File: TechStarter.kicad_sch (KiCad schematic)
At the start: 17 parts, among them J1 Conn_01x04_Socket, J2 Conn_01x04_Socket, U1 STM32F446RETx, U2 TMC2209-LA, U3 TMC2209-LA

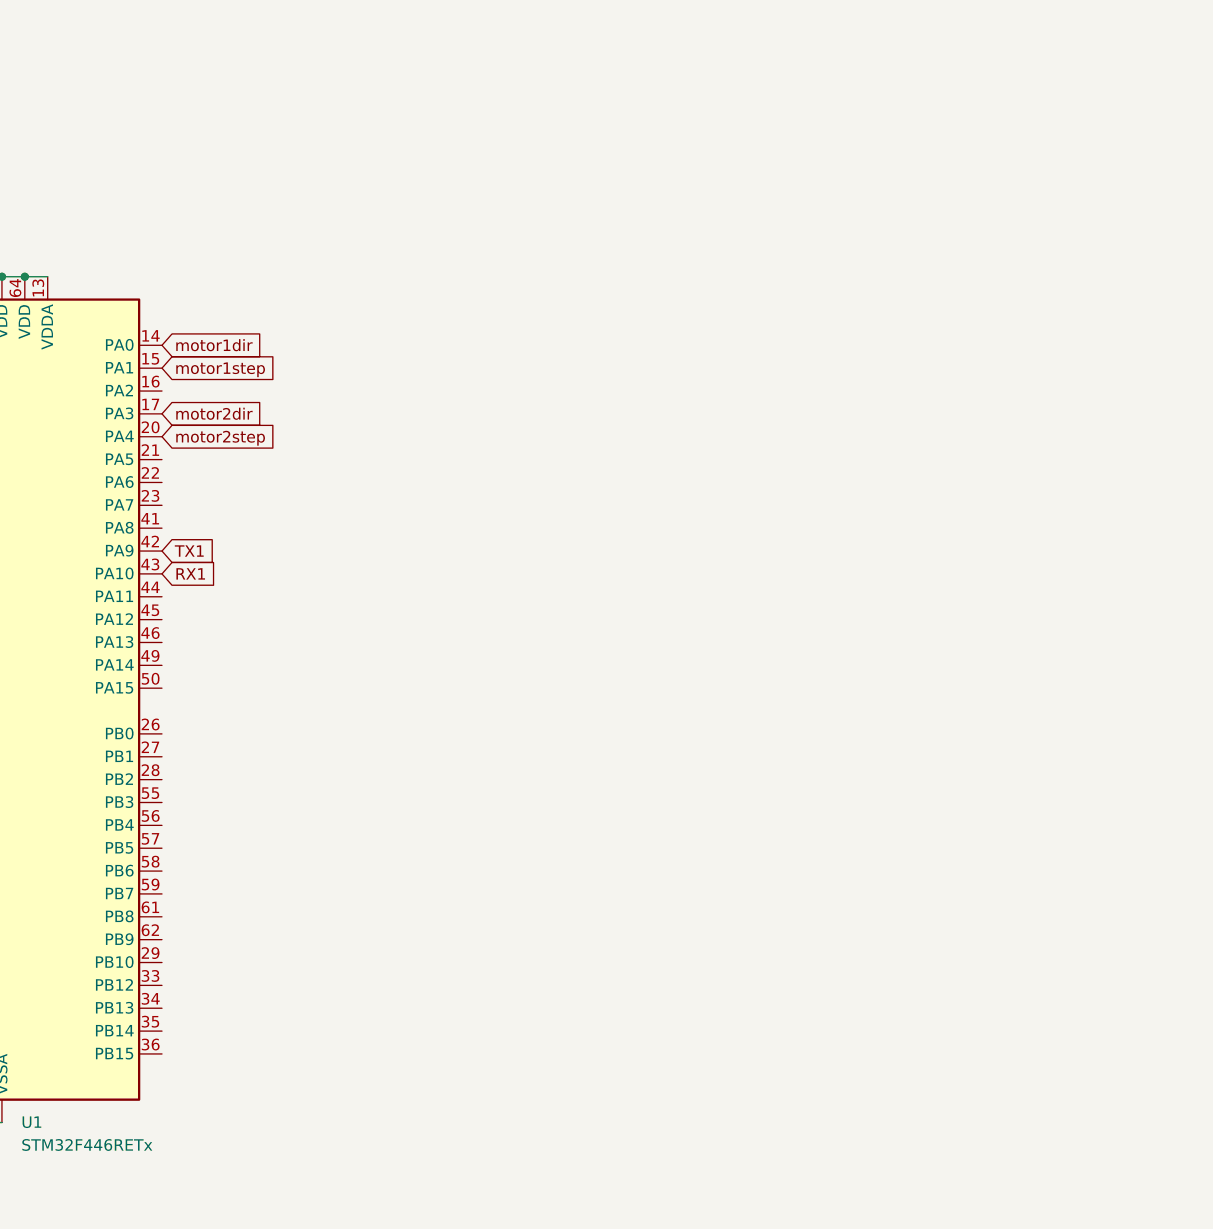
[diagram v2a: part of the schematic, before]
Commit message: MX25L3233FM1 (flash pamět)
Zapojil jsem flashku, měla by bejt lepčí než ta kterou jsem vybral předtím protože je větší a je NORová takže čtení je rychlejší než u NANDový
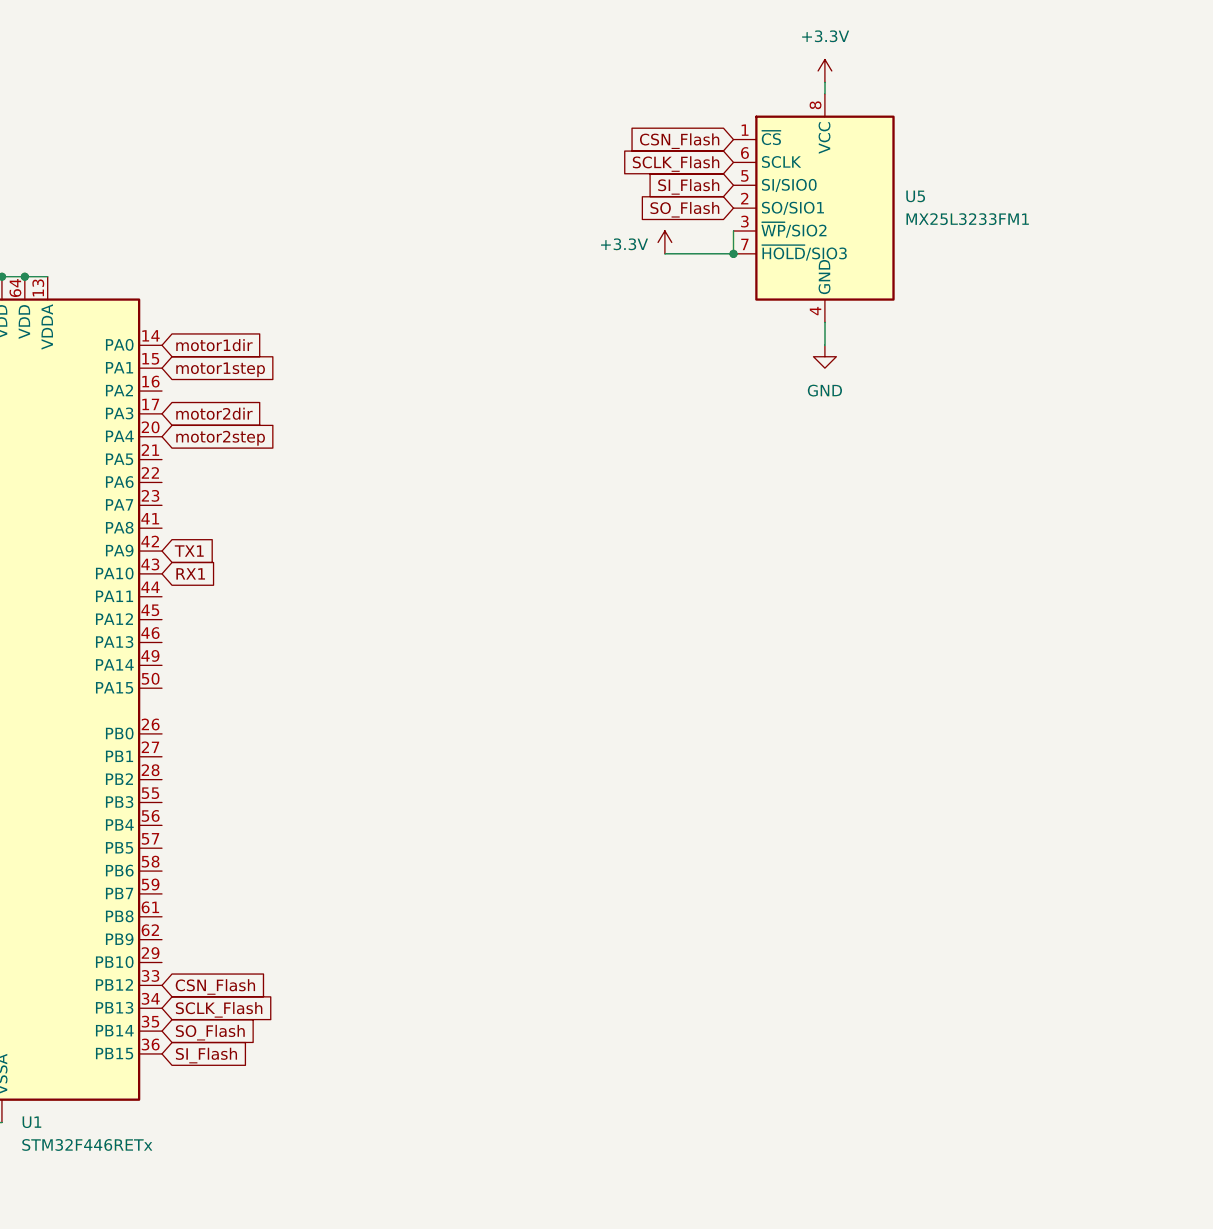
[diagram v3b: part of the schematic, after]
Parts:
- added U5: MX25L3233FM1, Package_SO:JEITA_SOIC-8_3.9x4.9mm_P1.27mm, symbol Memory_Flash:MX25L3233FM1
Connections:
- net +3.3V: now also U5.3 (~{WP}/SIO2), U5.7 (~{HOLD}/SIO3), U5.8 (VCC)
- net GND: now also U5.4 (GND)
- net CSN_Flash: now reaches U1.33 (PB12)
- net CSN_Flash: now also U5.1 (~{CS})
- net SCLK_Flash: now reaches U1.34 (PB13)
- net SCLK_Flash: now also U5.6 (SCLK)
- net SO_Flash: now reaches U1.35 (PB14)
- net SO_Flash: now also U5.2 (SO/SIO1)
- net SI_Flash: now reaches U1.36 (PB15)
- net SI_Flash: now also U5.5 (SI/SIO0)

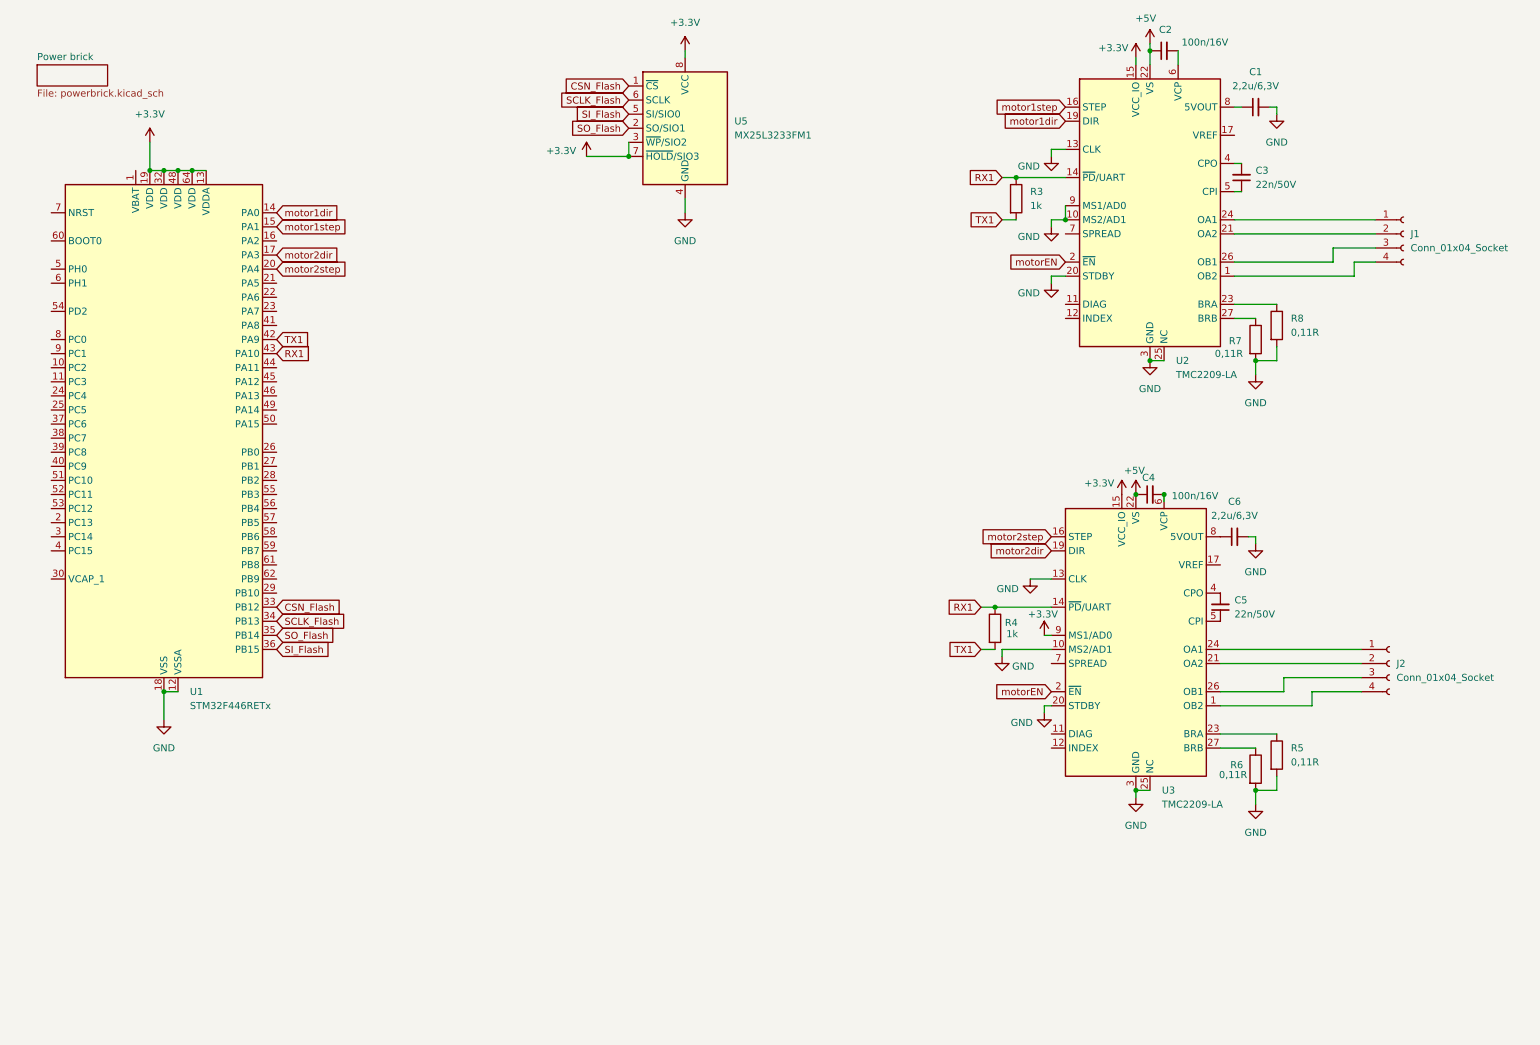
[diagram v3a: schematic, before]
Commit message: power to ICs
updated power brick. added CMOS battery
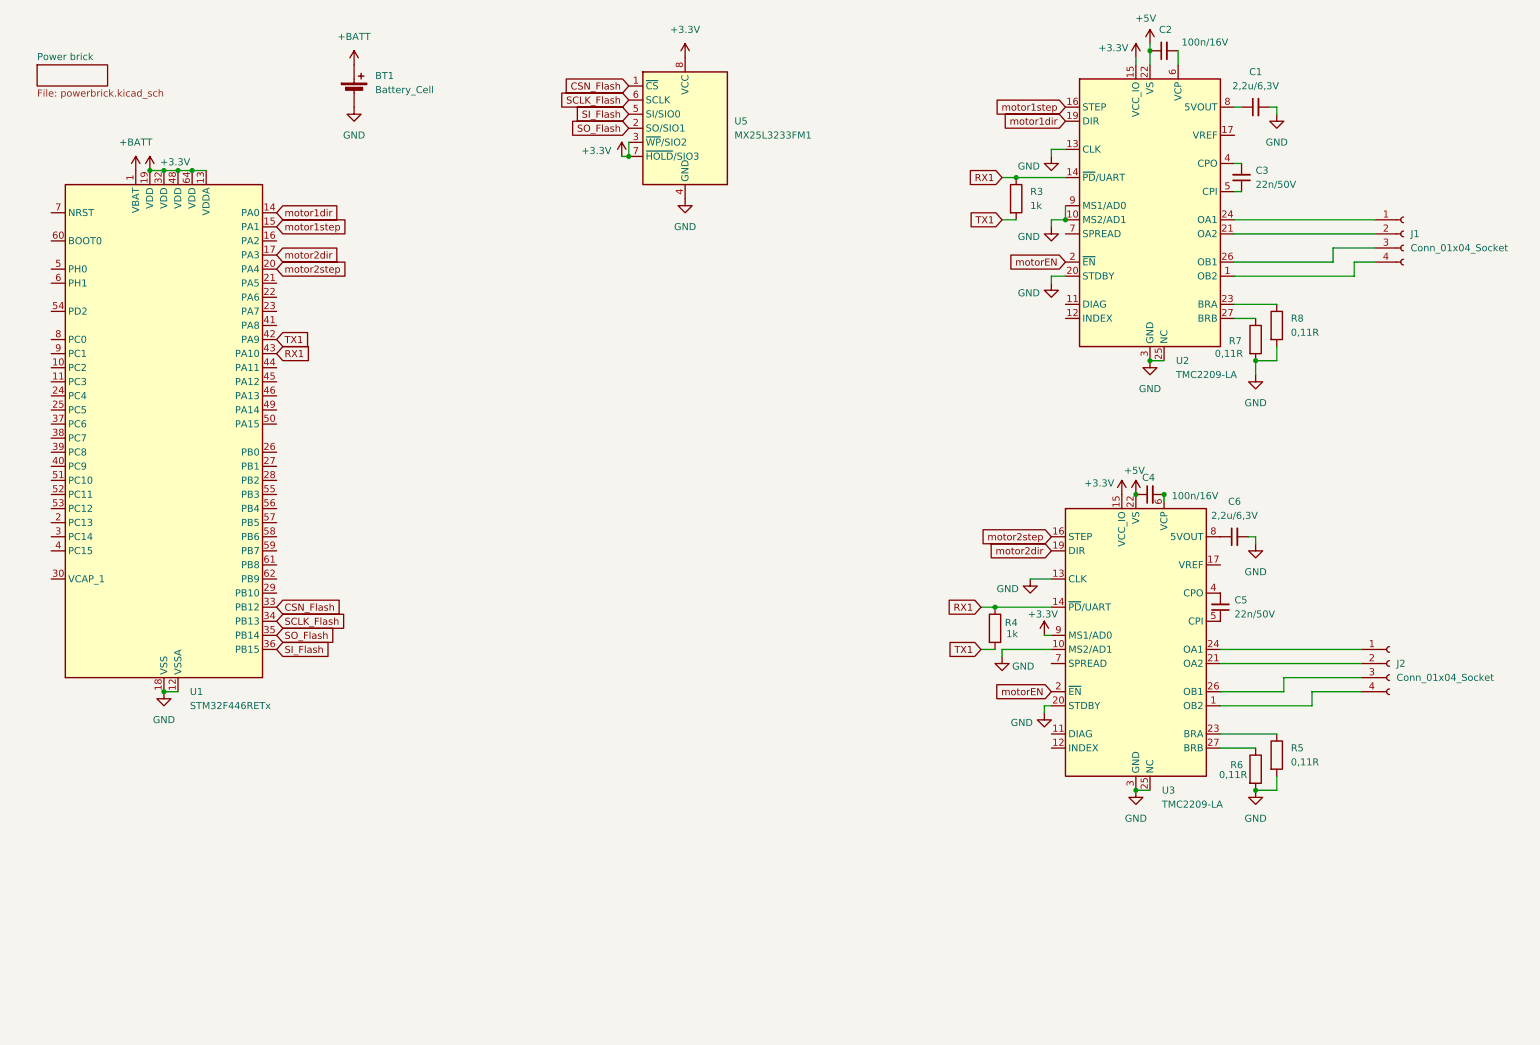
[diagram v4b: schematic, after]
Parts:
- added BT1: Battery_Cell, Battery:BatteryHolder_ComfortableElectronic_CH273-2450_1x2450, symbol Device:Battery_Cell
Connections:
- net GND: now also BT1.2 (-)
- net +BATT: now reaches U1.1 (VBAT)
- net +BATT: now also BT1.1 (+)

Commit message: connectors
added connectors for induction sensor, display, pneumatic motor and programming. programming and induction sensor connector isn't connected, pneumatic fully done, display connector unkown voltage for power
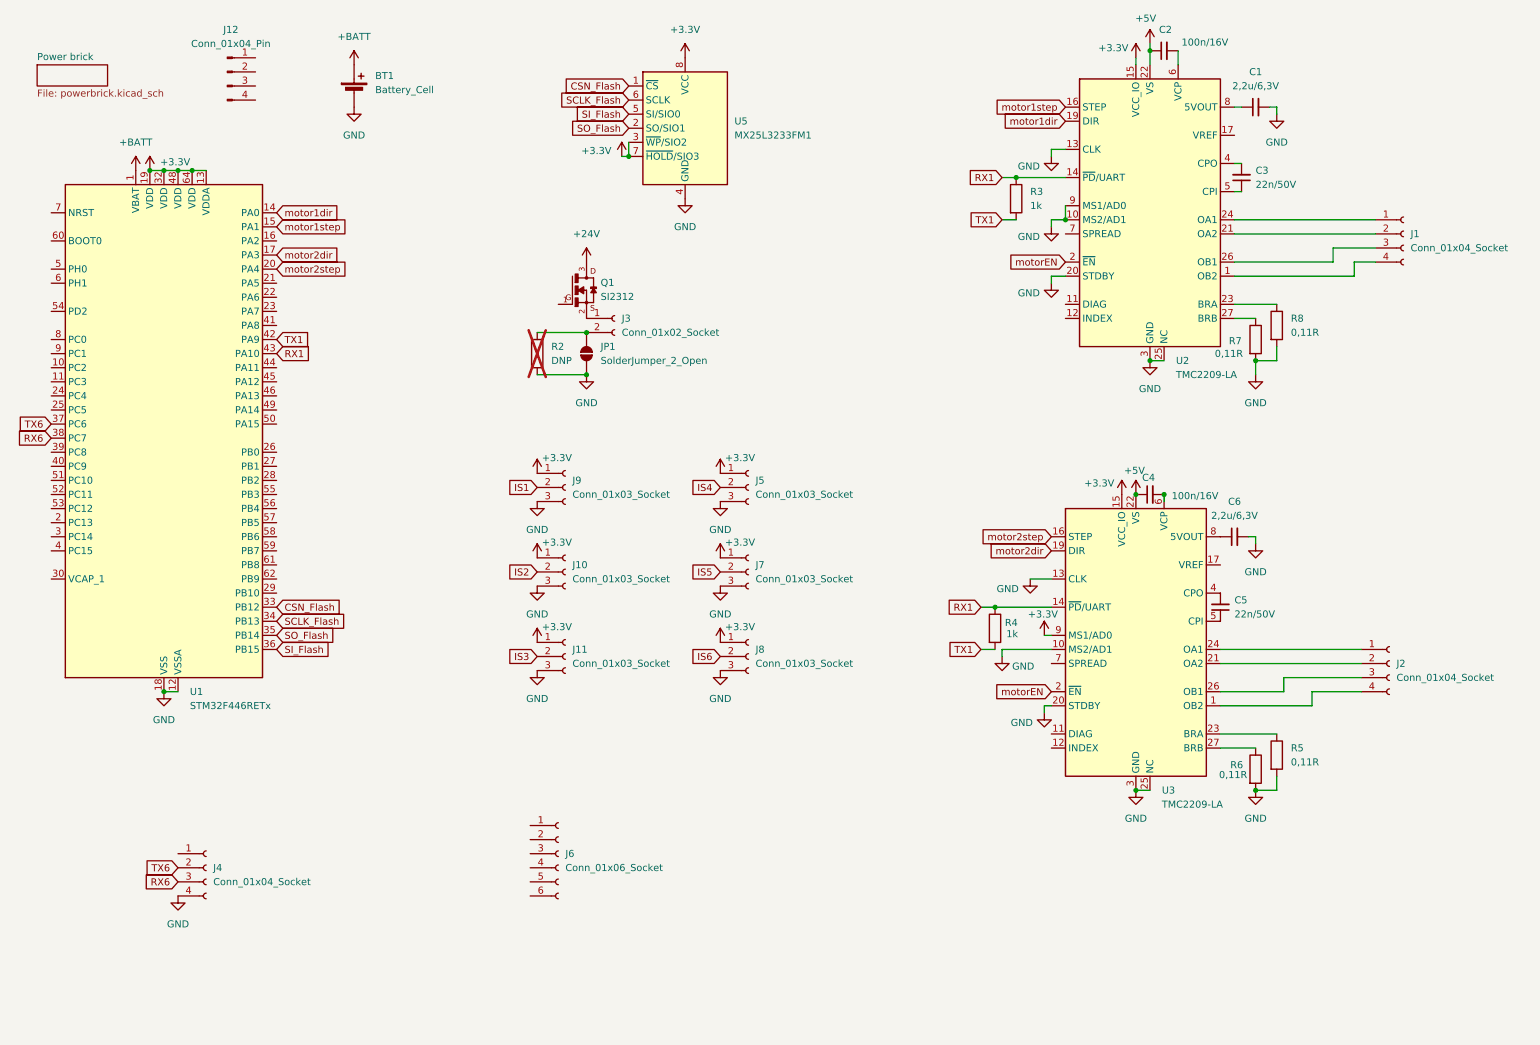
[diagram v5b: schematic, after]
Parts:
- added J10, J11, J5, J7, J8, J9: Conn_01x03_Socket, symbol Connector:Conn_01x03_Socket
- added J12: Conn_01x04_Pin, symbol Connector:Conn_01x04_Pin
- added J3: Conn_01x02_Socket, symbol Connector:Conn_01x02_Socket
- added J4: Conn_01x04_Socket, symbol Connector:Conn_01x04_Socket
- added J6: Conn_01x06_Socket, symbol Connector:Conn_01x06_Socket
- added JP1: SolderJumper_2_Open, symbol Jumper:SolderJumper_2_Open
- added Q1: SI2312, SI2312:SOT23, symbol SI2312:SI2312
- added R2: DNP, symbol Device:R
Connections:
- net +3.3V: now also J10.1 (Pin_1), J11.1 (Pin_1), J5.1 (Pin_1), J7.1 (Pin_1), J8.1 (Pin_1), J9.1 (Pin_1)
- net GND: now also J10.3 (Pin_3), J11.3 (Pin_3), J4.4 (Pin_4), J5.3 (Pin_3), J7.3 (Pin_3), J8.3 (Pin_3), J9.3 (Pin_3), JP1.1 (A), R2.2
- net TX6: now reaches U1.37 (PC6)
- net TX6: now also J4.2 (Pin_2)
- net RX6: now reaches U1.38 (PC7)
- net RX6: now also J4.3 (Pin_3)
- new net: J3.2 (Pin_2), JP1.2 (B), R2.1
- new net: J3.1 (Pin_1), Q1.2
- new net +24V: Q1.3
- new net IS1: J9.2 (Pin_2)
- new net IS2: J10.2 (Pin_2)
- new net IS3: J11.2 (Pin_2)
- new net IS4: J5.2 (Pin_2)
- new net IS5: J7.2 (Pin_2)
- new net IS6: J8.2 (Pin_2)

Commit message: .
finishing connectors
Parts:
- removed J6: Conn_01x06_Socket, symbol Connector:Conn_01x06_Socket
- added J6: Conn_01x04_Socket, symbol Connector:Conn_01x04_Socket
- C1, J10, J11, J5, J7, J8, J9: footprint (none) -> Connector_JST:JST_XH_S3B-XH-A_1x03_P2.50mm_Horizontal
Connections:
- net +3.3V: now also J12.1 (Pin_1), J6.1 (Pin_1), J6.3 (Pin_3)
- net +5V: now also J4.1 (Pin_1)
- net GND: now also J12.4 (Pin_4)
- net IS1: now also U1.26 (PB0)
- net IS2: now also U1.27 (PB1)
- net IS3: now also U1.28 (PB2)
- net IS4: now also U1.55 (PB3)
- net IS5: now also U1.56 (PB4)
- net IS6: now also U1.57 (PB5)
- net SWDIO: now reaches J12.2 (Pin_2)
- net SWDIO: now also U1.46 (PA13)
- net SWCLK: now reaches J12.3 (Pin_3)
- net SWCLK: now also U1.49 (PA14)
- net at Q1.1: now also U1.16 (PA2)
- net EB1: now reaches U1.58 (PB6)
- net EB1: now also J6.2 (Pin_2)
- net EB2: now reaches U1.59 (PB7)
- net EB2: now also J6.4 (Pin_4)
